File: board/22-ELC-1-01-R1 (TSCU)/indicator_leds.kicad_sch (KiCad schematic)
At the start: 21 parts, among them U12 LM358, U13 LM358, U14 LM358

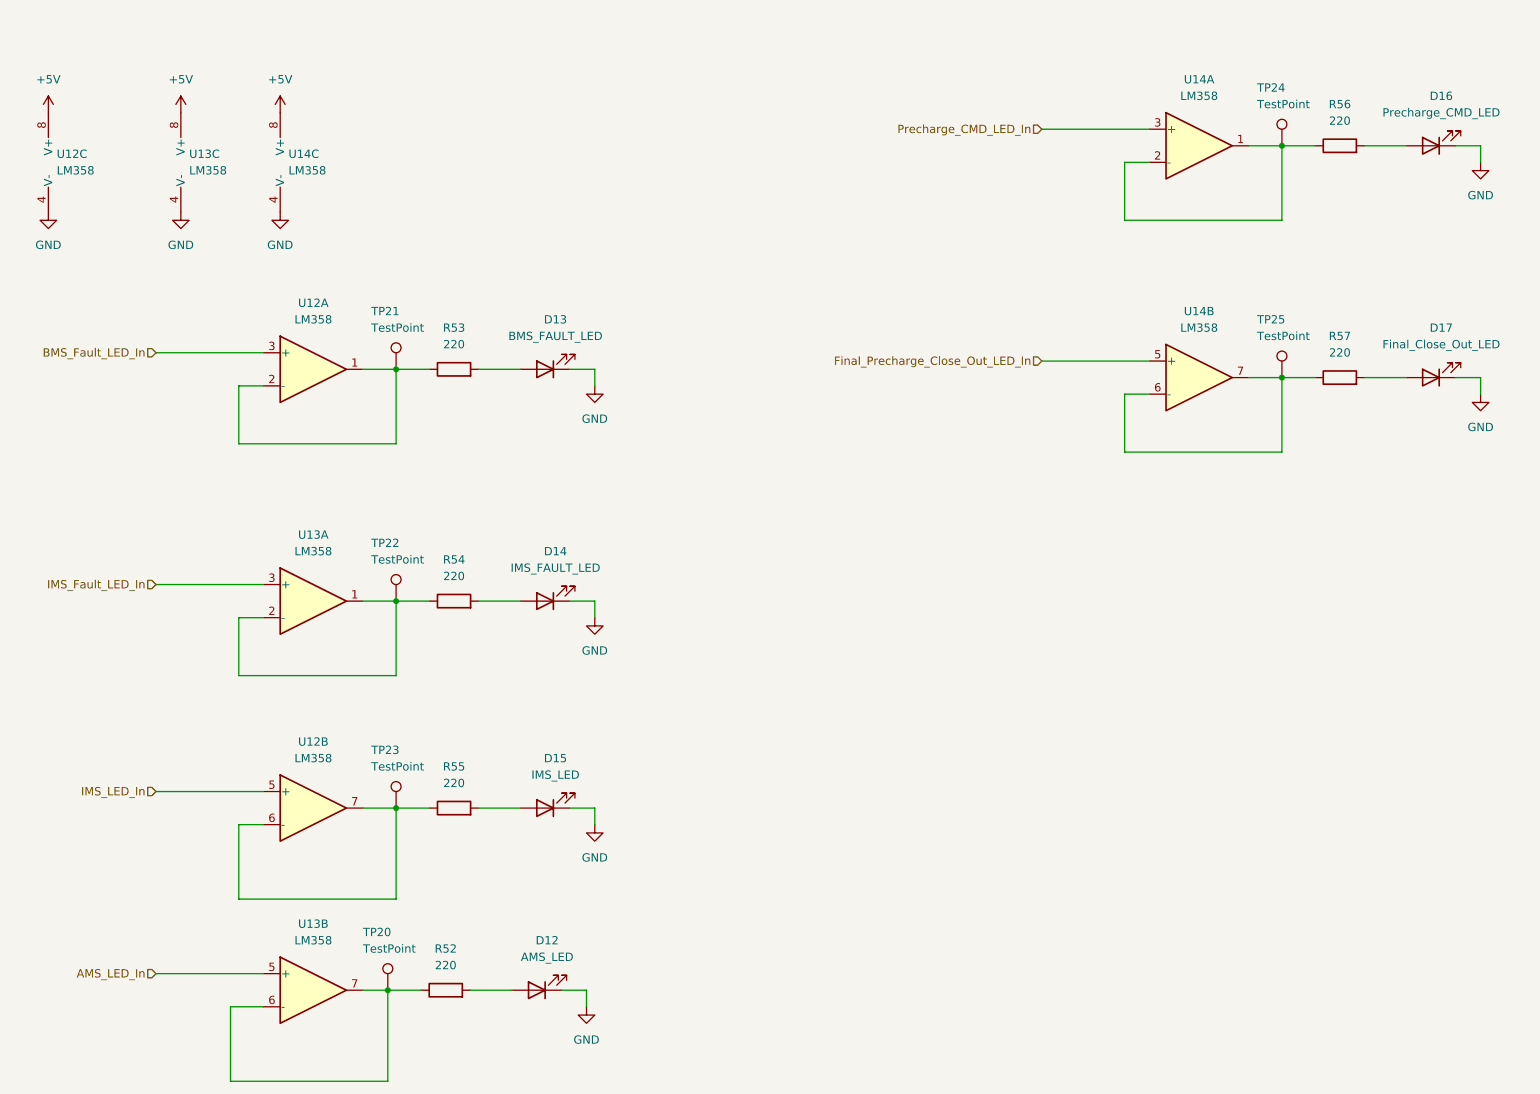
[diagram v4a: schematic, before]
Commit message: All good except need to switch everything to accepting 24v power
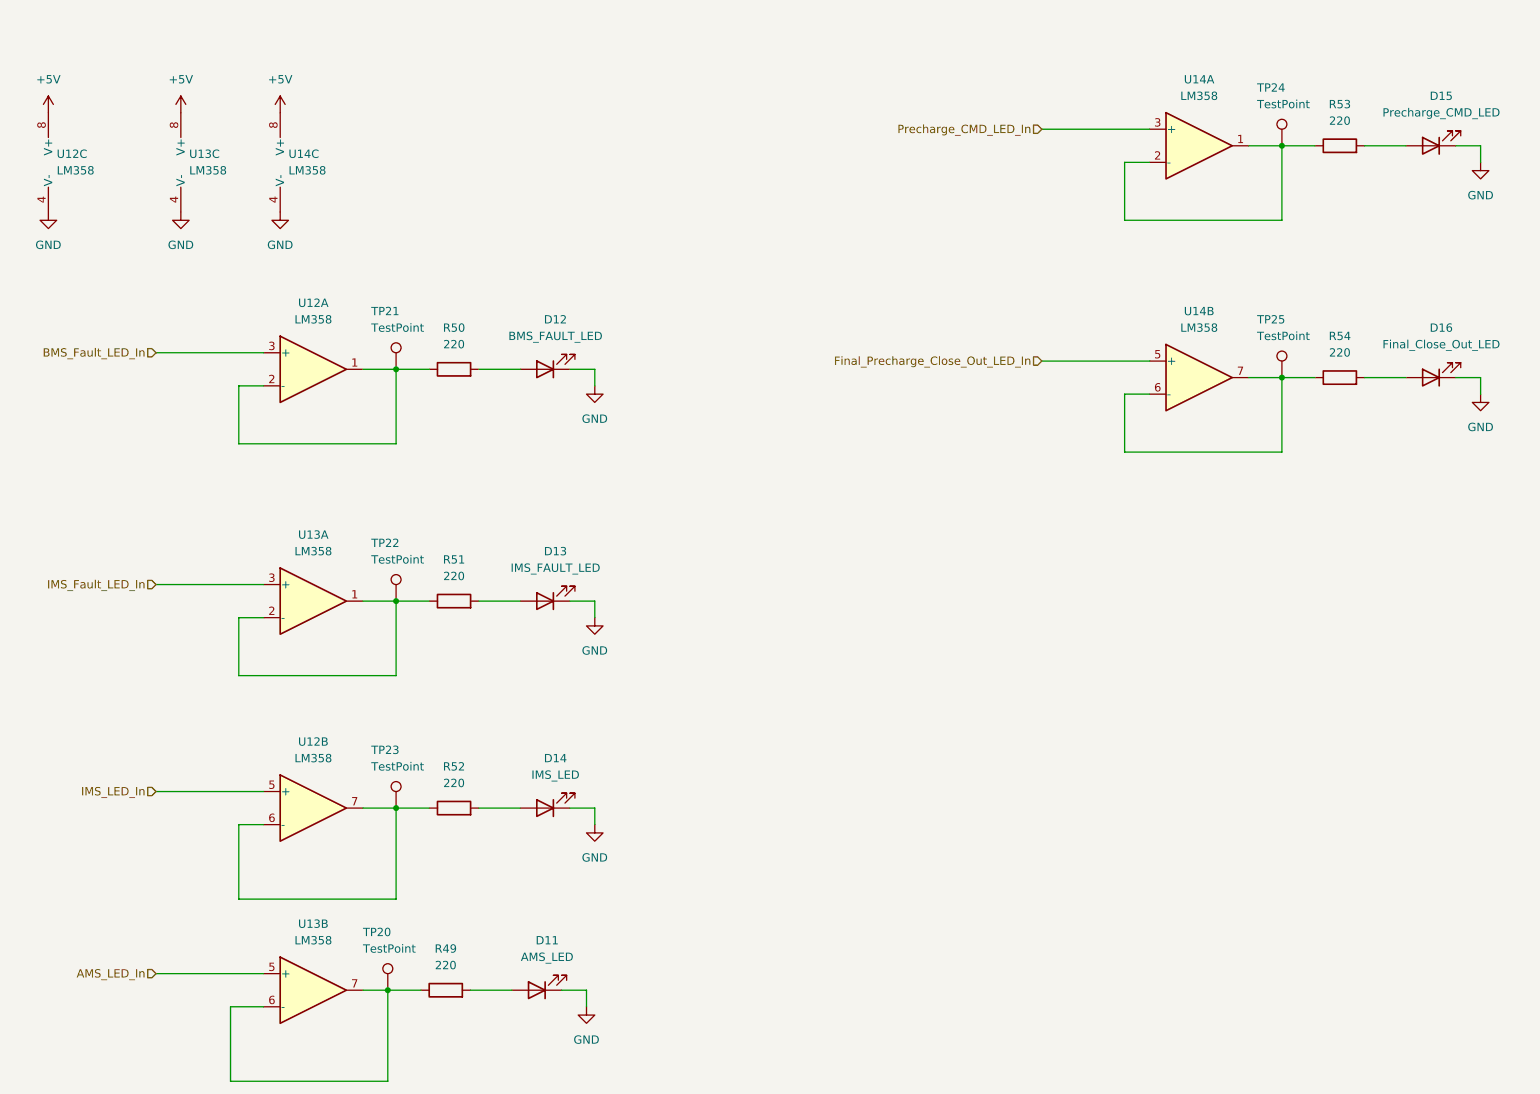
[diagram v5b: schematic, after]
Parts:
- D11: renamed from D12; footprint (none) -> LED_SMD:LED_1206_3216Metric
- D12: renamed from D13; footprint (none) -> LED_SMD:LED_1206_3216Metric
- D13: renamed from D14; footprint (none) -> LED_SMD:LED_1206_3216Metric
- D14: renamed from D15; footprint (none) -> LED_SMD:LED_1206_3216Metric
- D15: renamed from D16; footprint (none) -> LED_SMD:LED_1206_3216Metric
- D16: renamed from D17; footprint (none) -> LED_SMD:LED_1206_3216Metric
- R49: renamed from R52; footprint (none) -> Resistor_SMD:R_0603_1608Metric_Pad0.98x0.95mm_HandSolder
- R50: renamed from R53; footprint (none) -> Resistor_SMD:R_0603_1608Metric_Pad0.98x0.95mm_HandSolder
- R51: renamed from R54; footprint (none) -> Resistor_SMD:R_0603_1608Metric_Pad0.98x0.95mm_HandSolder
- R52: renamed from R55; footprint (none) -> Resistor_SMD:R_0603_1608Metric_Pad0.98x0.95mm_HandSolder
- R53: renamed from R56; footprint (none) -> Resistor_SMD:R_0603_1608Metric_Pad0.98x0.95mm_HandSolder
- R54: renamed from R57; footprint (none) -> Resistor_SMD:R_0603_1608Metric_Pad0.98x0.95mm_HandSolder
- TP20, TP21, TP22, TP23, TP24, TP25: footprint (none) -> TestPoint:TestPoint_THTPad_D1.0mm_Drill0.5mm
- U12, U13, U14: footprint (none) -> Package_SO:SOIC-8_3.9x4.9mm_P1.27mm

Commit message: Finalized schematic, started board layout
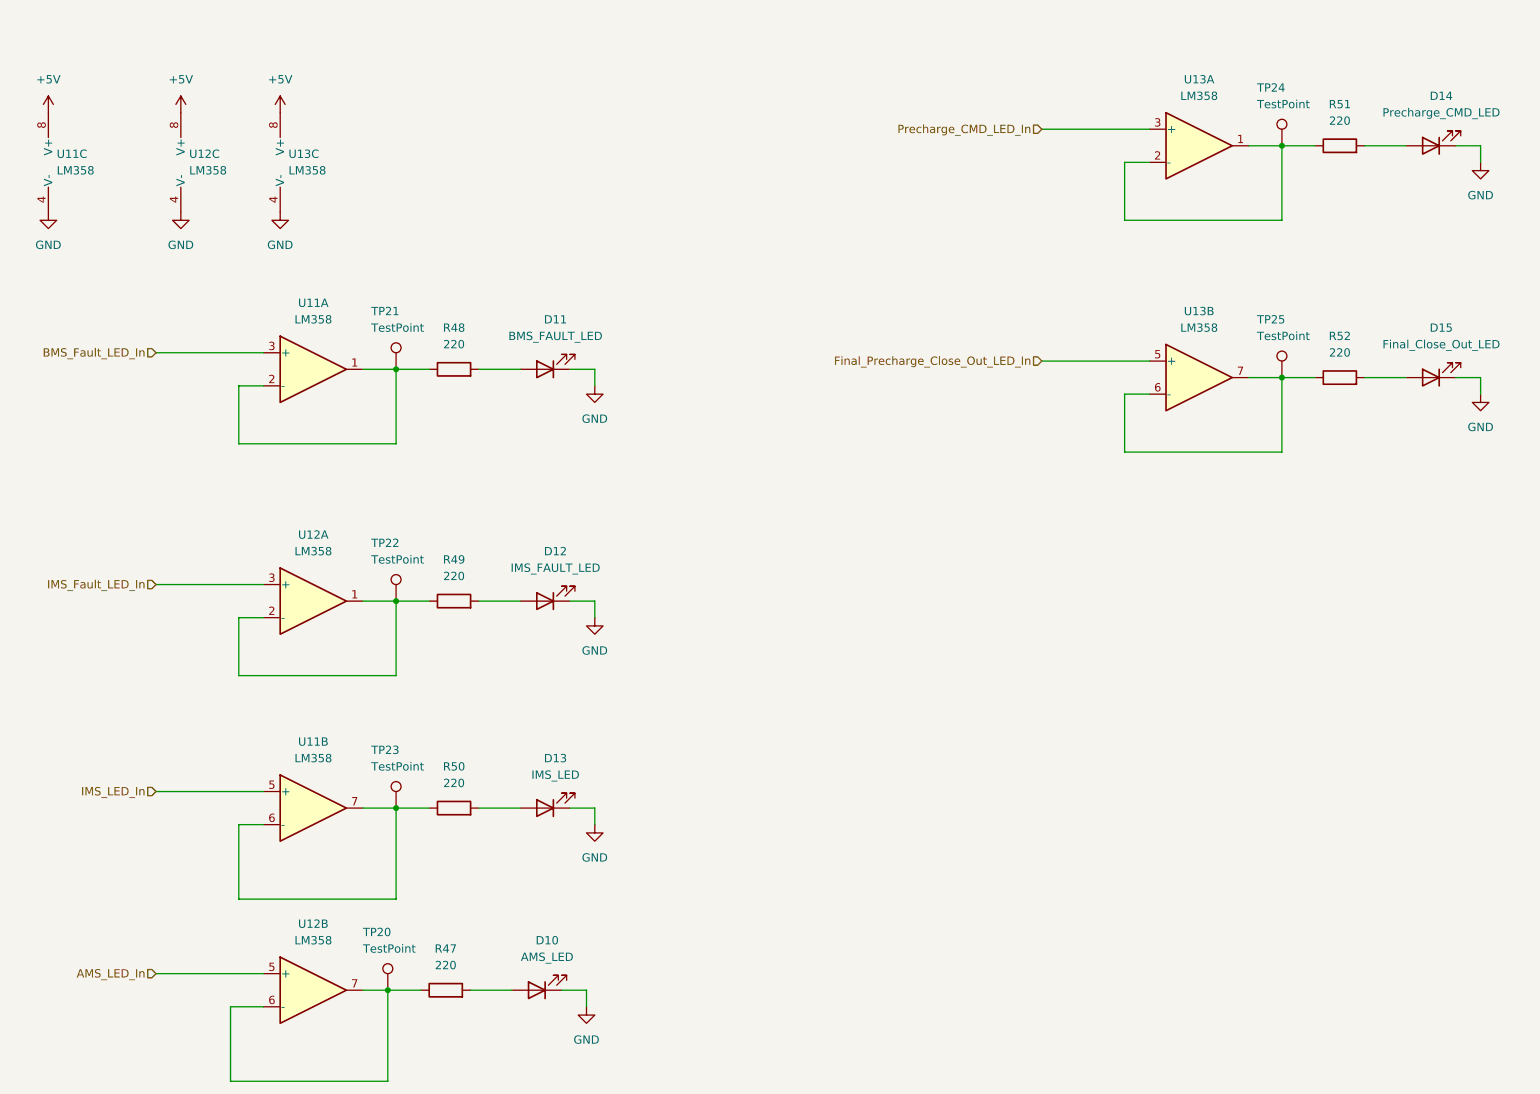
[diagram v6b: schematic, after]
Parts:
- R47: renamed from R49; footprint Resistor_SMD:R_0603_1608Metric_Pad0.98x0.95mm_HandSolder -> FixedTextSizes:R_0402_1005Metric
- R48: renamed from R50; footprint Resistor_SMD:R_0603_1608Metric_Pad0.98x0.95mm_HandSolder -> FixedTextSizes:R_0402_1005Metric
- R49: renamed from R51; footprint Resistor_SMD:R_0603_1608Metric_Pad0.98x0.95mm_HandSolder -> FixedTextSizes:R_0402_1005Metric
- R50: renamed from R52; footprint Resistor_SMD:R_0603_1608Metric_Pad0.98x0.95mm_HandSolder -> FixedTextSizes:R_0402_1005Metric
- R51: renamed from R53; footprint Resistor_SMD:R_0603_1608Metric_Pad0.98x0.95mm_HandSolder -> FixedTextSizes:R_0402_1005Metric
- R52: renamed from R54; footprint Resistor_SMD:R_0603_1608Metric_Pad0.98x0.95mm_HandSolder -> FixedTextSizes:R_0402_1005Metric
- renumbered D11 to D10, D12 to D11, D13 to D12, D14 to D13, D15 to D14, D16 to D15, U12 to U11, U13 to U12, U14 to U13

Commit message: More progress
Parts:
- removed D10: AMS_LED, LED_SMD:LED_1206_3216Metric, symbol Device:LED
- removed D13: IMS_LED, LED_SMD:LED_1206_3216Metric, symbol Device:LED
- removed R47, R48, R49, R50: 220, FixedTextSizes:R_0402_1005Metric, symbol Device:R
- removed TP20, TP21, TP22, TP23, TP24, TP25: TestPoint, TestPoint:TestPoint_THTPad_D1.0mm_Drill0.5mm, symbol Connector:TestPoint
- removed unit 2 of U11
- removed unit 1 of U11
- removed unit 1 of U12
- removed unit 2 of U12
- removed unit 1 of U13
- removed unit 2 of U13
- added Q? (x4): AO3400A, Package_TO_SOT_SMD:SOT-23, symbol Device:Q_NMOS_GSD
- added R? (x4): 10k, FixedTextSizes:R_0402_1005Metric, symbol Device:R
- added R? (x4): 100k, FixedTextSizes:R_0402_1005Metric, symbol Device:R
- added R? (x2): 220, FixedTextSizes:R_0402_1005Metric, symbol Device:R
- added TP? (x4): TestPoint, TestPoint:TestPoint_THTPad_D1.0mm_Drill0.5mm, symbol Connector:TestPoint
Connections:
- net BMS_Fault_LED_In: now also R?.1
- net Final_Precharge_Close_Out_LED_In: now also R?.1
- net GND: now also Q?.2 (S), Q?.2 (S), Q?.2 (S), Q?.2 (S), R?.2, R?.2, R?.2, R?.2
- net IMS_Fault_LED_In: now also R?.1
- net Precharge_CMD_LED_In: now also R?.1
- net at R51.1: now also Q?.3 (D), TP?.1
- net at D11.2 (A): now also R?.2
- net at D12.2 (A): now also R?.2
- net at R52.1: now also Q?.3 (D), TP?.1
- new net: Q?.1 (G), R?.1, R?.2 (x4)
- new net: Q?.3 (D), R?.1, TP?.1 (x2)
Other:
- moved on the sheet: D11, D12, D14, D15, R51, R52
